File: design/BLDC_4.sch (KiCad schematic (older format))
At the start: 32 parts, among them K1 SERVO, P1 CANBUS, P10 MOTOR3, P11 MOTOR2, P12 MOTOR1, P2 HALL/Encoder, P3 HALL/Encoder, P4 PWR_COMM, P5 IN+, P6 IN-, P7 MOTOR3, P8 MOTOR2, P9 MOTOR1, X1 MINI-USB-SHIELD-32005-201

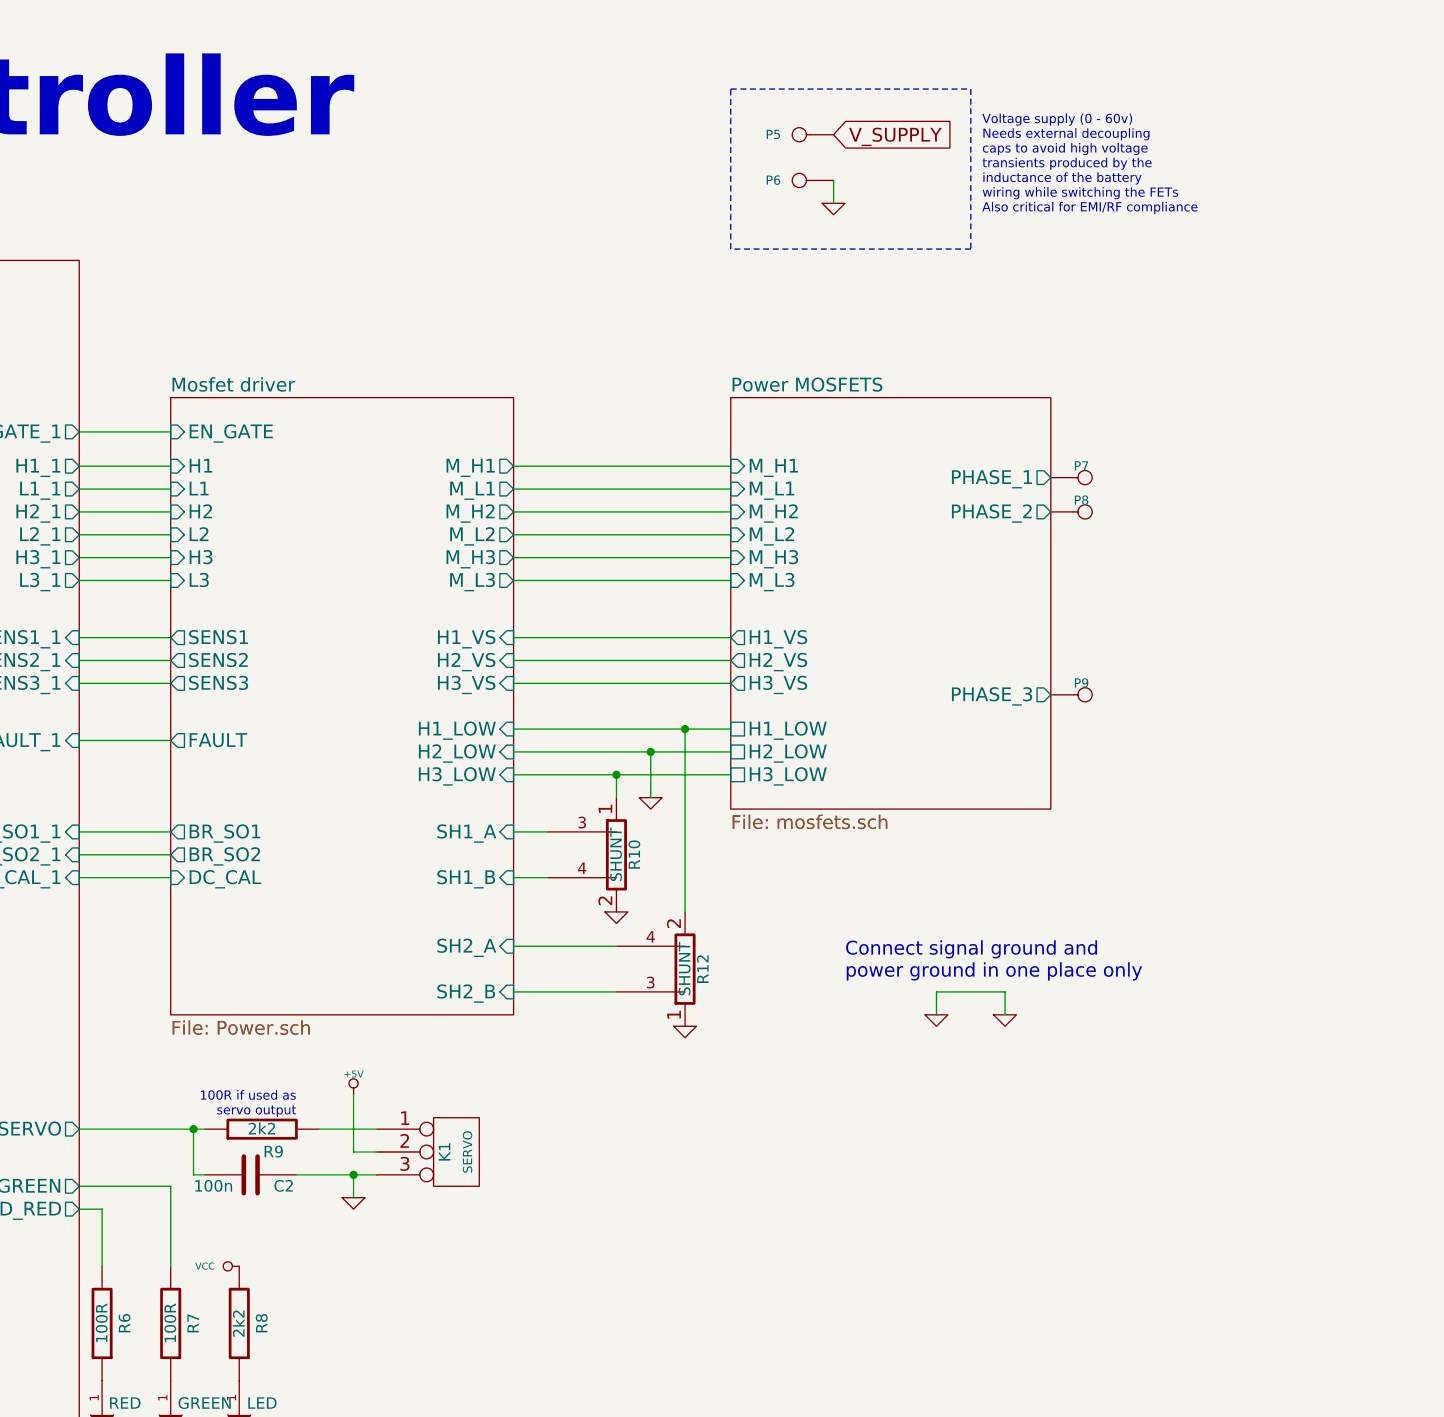
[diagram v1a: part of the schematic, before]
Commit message: Declare mosfet supply
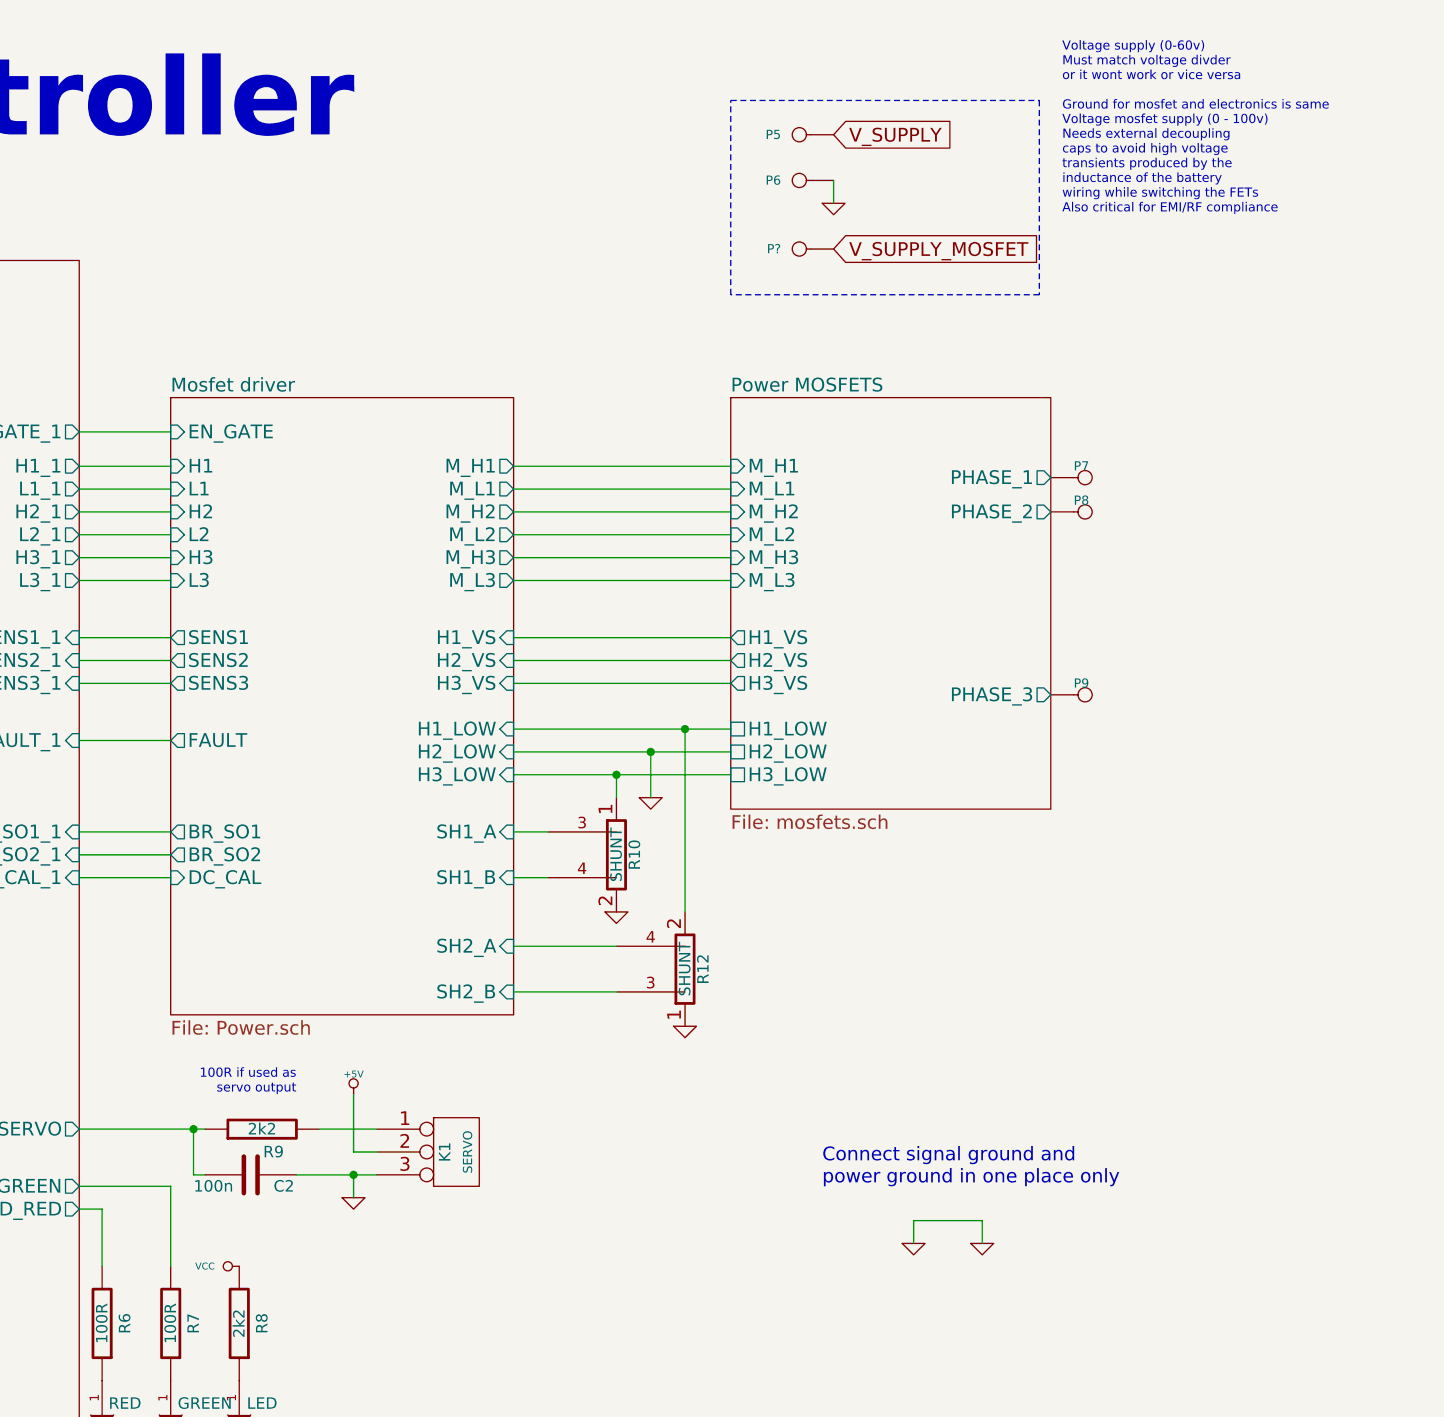
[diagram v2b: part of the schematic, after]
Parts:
- added P?: IN+, CRF1:1PAD_4x5mm, symbol CONN_1
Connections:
- new net V_SUPPLY_MOSFET: P?.1
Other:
- note added: "Voltage mosfet supply (0 - 100v)\nNeeds external decoupling\ncaps to avoid high voltage\ntransients produced by the\ninductance of the battery\nwiring while switching the FETs\nAlso critical for EMI/RF compliance"
- note added: "Voltage supply (0-60v)\nMust match voltage divder\nor it wont work or vice versa\n\nGround for mosfet and electronics is same"
- note removed: "Voltage supply (0 - 60v)\nNeeds external decoupling\ncaps to avoid high voltage\ntransients produced by the\ninductance of the battery\nwiring while switching the FETs\nAlso critical for EMI/RF compliance"
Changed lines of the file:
@@
 $EndComp
 $Comp
-L +5V #PWR01
+L +5V #PWR3
 U 1 1 522DA04D
 P 2850 5050
-F 0 "#PWR01" H 2850 5140 20  0001 C CNN
+F 0 "#PWR3" H 2850 5140 20  0001 C CNN
 F 1 "+5V" V 2800 5100 30  0000 C CNN
 F 2 "" H 2850 5050 60  0001 C CNN
@@
 $EndComp
 $Comp
-L GND #PWR02
+L GND #PWR6
 U 1 1 522DA053
 P 2900 4550
-F 0 "#PWR02" H 2900 4550 30  0001 C CNN
+F 0 "#PWR6" H 2900 4550 30  0001 C CNN
 F 1 "GND" H 2900 4480 30  0001 C CNN
 F 2 "" H 2900 4550 60  0001 C CNN
@@
 $EndComp
 $Comp
-L GND #PWR03
+L GND #PWR18
 U 1 1 522DA0BA
 P 8400 6000
-F 0 "#PWR03" H 8400 6000 30  0001 C CNN
+F 0 "#PWR18" H 8400 6000 30  0001 C CNN
 F 1 "GND" H 8400 5930 30  0001 C CNN
 F 2 "" H 8400 6000 60  0001 C CNN
@@
 V_SUPPLY
 $Comp
-L GND #PWR04
+L GND #PWR11
 U 1 1 522DA0CE
 P 3100 2650
-F 0 "#PWR04" H 3100 2650 30  0001 C CNN
+F 0 "#PWR11" H 3100 2650 30  0001 C CNN
 F 1 "GND" H 3100 2580 30  0001 C CNN
 F 2 "" H 3100 2650 60  0001 C CNN
@@
 $EndComp
 $Comp
-L GND #PWR05
+L GND #PWR5
 U 1 1 522DA0E2
 P 2850 6950
-F 0 "#PWR05" H 2850 6950 30  0001 C CNN
+F 0 "#PWR5" H 2850 6950 30  0001 C CNN
 F 1 "GND" H 2850 6880 30  0001 C CNN
 F 2 "" H 2850 6950 60  0001 C CNN
@@
 $EndComp
 $Comp
-L GND #PWR06
+L GND #PWR10
 U 1 1 522DA0FC
 P 3000 3600
-F 0 "#PWR06" H 3000 3600 30  0001 C CNN
+F 0 "#PWR10" H 3000 3600 30  0001 C CNN
 F 1 "GND" H 3000 3530 30  0001 C CNN
 F 2 "" H 3000 3600 60  0001 C CNN
@@
 $EndComp
 $Comp
-L +5V #PWR07
+L +5V #PWR8
 U 1 1 522DA11A
 P 2950 6750
-F 0 "#PWR07" H 2950 6840 20  0001 C CNN
+F 0 "#PWR8" H 2950 6840 20  0001 C CNN
 F 1 "+5V" V 2950 6900 30  0000 C CNN
 F 2 "" H 2950 6750 60  0001 C CNN
@@
 $EndComp
 $Comp
-L VCC #PWR08
+L VCC #PWR9
 U 1 1 522DA120
 P 2950 6850
-F 0 "#PWR08" H 2950 6950 30  0001 C CNN
+F 0 "#PWR9" H 2950 6950 30  0001 C CNN
 F 1 "VCC" V 2950 7000 30  0000 C CNN
 F 2 "" H 2950 6850 60  0001 C CNN
@@
 $EndComp
 $Comp
-L +5V #PWR09
+L +5V #PWR17
 U 1 1 522DA158
 P 8400 5550
-F 0 "#PWR09" H 8400 5640 20  0001 C CNN
+F 0 "#PWR17" H 8400 5640 20  0001 C CNN
 F 1 "+5V" H 8400 5640 30  0000 C CNN
 F 2 "" H 8400 5550 60  0001 C CNN
@@
 	-1   0    0    -1
 $EndComp
-Text Notes 8150 5650 2    40   ~ 0
+Text Notes 8150 5550 2    40   ~ 0
 100R if used as\nservo output
 $Comp
@@
 $EndComp
 $Comp
-L +5V #PWR010
+L +5V #PWR12
 U 1 1 522DA254
 P 4200 3050
-F 0 "#PWR010" H 4200 3140 20  0001 C CNN
+F 0 "#PWR12" H 4200 3140 20  0001 C CNN
 F 1 "+5V" H 4200 3140 30  0000 C CNN
 F 2 "" H 4200 3050 60  0001 C CNN
@@
 $EndComp
 $Comp
-L GND #PWR011
+L GND #PWR26
 U 1 1 53FA1F8F
-P 10950 5200
-F 0 "#PWR011" H 10950 5200 30  0001 C CNN
-F 1 "GND" H 10950 5130 30  0001 C CNN
-F 2 "" H 10950 5200 60  0001 C CNN
-F 3 "" H 10950 5200 60  0001 C CNN
-	1    10950 5200
+P 10850 6200
+F 0 "#PWR26" H 10850 6200 30  0001 C CNN
+F 1 "GND" H 10850 6130 30  0001 C CNN
+F 2 "" H 10850 6200 60  0001 C CNN
+F 3 "" H 10850 6200 60  0001 C CNN
+	1    10850 6200
 	1    0    0    -1
 $EndComp
@@
 C8 C8 08 D2 A9 87 39 1B F9 3D 64 10 3C A5 22 3B 19 76 2F 98 2B 2B 2B 1E 8F A7 AB AB 0B FB AC 1D
 B9 73 C8 EF 2C EC 8D 33 57 03 96 70 05 29 43 0C 6A C5 A8 D7 30 9E 87 2D DE BE E8 EA 73 2F 9C 18
-F1 B3 C3 9F 6D FA 1E FF 03 71 17 46 7E 55 DF FF 4E 00 00 00 00 49 45 4E 44 AE 42 60 82 35 $EndBitmap
+F1 B3 C3 9F 6D FA 1E FF 03 71 17 46 7E 55 DF FF 4E 00 00 00 00 49 45 4E 44 AE 42 60 82 1A $EndBitmap
 EndData
 $EndBitmap
@@
 $EndSheet
 $Comp
-L GND #PWR012
+L GND #PWR2
 U 1 1 53FB6DA8
 P 2850 4200
-F 0 "#PWR012" H 2850 4200 30  0001 C CNN
+F 0 "#PWR2" H 2850 4200 30  0001 C CNN
 F 1 "GND" H 2850 4130 30  0001 C CNN
 F 2 "" H 2850 4200 60  0001 C CNN
@@
 	0    1    1    0
 $EndComp
-Text Notes 11150 1700 0    40   ~ 0
-Voltage supply (0 - 60v)\nNeeds external decoupling\ncaps to avoid high voltage\ntransients produced by the\ninductance of the battery\nwiring while switching the FETs\nAlso critical for EMI/RF compliance
+Text Notes 11500 1700 0    40   ~ 0
+Voltage mosfet supply (0 - 100v)\nNeeds external decoupling\ncaps to avoid high voltage\ntransients produced by the\ninductance of the battery\nwiring while switching the FETs\nAlso critical for EMI/RF compliance
 $Comp
 L R R6
@@
 $EndComp
 $Comp
-L GND #PWR013
+L GND #PWR13
 U 1 1 53FC021C
 P 7300 7200
-F 0 "#PWR013" H 7300 7200 30  0001 C CNN
+F 0 "#PWR13" H 7300 7200 30  0001 C CNN
 F 1 "GND" H 7300 7130 30  0001 C CNN
 F 2 "" H 7300 7200 60  0001 C CNN
@@
 $EndComp
 $Comp
-L GND #PWR014
+L GND #PWR14
 U 1 1 53FC131A
 P 7600 7200
-F 0 "#PWR014" H 7600 7200 30  0001 C CNN
+F 0 "#PWR14" H 7600 7200 30  0001 C CNN
 F 1 "GND" H 7600 7130 30  0001 C CNN
 F 2 "" H 7600 7200 60  0001 C CNN
@@
 $EndComp
 $Comp
-L GND #PWR015
+L GND #PWR16
 U 1 1 53FC8AA4
 P 7900 7200
-F 0 "#PWR015" H 7900 7200 30  0001 C CNN
+F 0 "#PWR16" H 7900 7200 30  0001 C CNN
 F 1 "GND" H 7900 7130 30  0001 C CNN
 F 2 "" H 7900 7200 60  0001 C CNN
@@
 $EndComp
 $Comp
-L VCC #PWR016
+L VCC #PWR15
 U 1 1 53FC98D2
 P 7900 6300
-F 0 "#PWR016" H 7900 6400 30  0001 C CNN
+F 0 "#PWR15" H 7900 6400 30  0001 C CNN
 F 1 "VCC" V 7900 6450 30  0000 C CNN
 F 2 "" H 7900 6300 60  0001 C CNN
@@
 Connection ~ 9700 4050
 Wire Wire Line
-	10950 5100 10950 5200
+	10850 6100 10850 6200
 Wire Wire Line
-	11250 5100 11250 5200
+	11150 6100 11150 6200
 Wire Wire Line
 	10500 1650 10500 1550
@@
 Wire Wire Line
 	4050 3300 4650 3300
-Wire Notes Line
-	10050 1150 11100 1150
-Wire Notes Line
-	11100 1150 11100 1850
-Wire Notes Line
-	11100 1850 10050 1850
-Wire Notes Line
-	10050 1850 10050 1150
 Wire Wire Line
 	7300 6050 7300 6300
@@
 $EndComp
 $Comp
-L +5V #PWR017
+L +5V #PWR1
 U 1 1 54036995
 P 2850 3900
-F 0 "#PWR017" H 2850 3990 20  0001 C CNN
+F 0 "#PWR1" H 2850 3990 20  0001 C CNN
 F 1 "+5V" H 2850 3990 30  0000 C CNN
 F 2 "" H 2850 3900 60  0001 C CNN
@@
 $EndComp
 Wire Wire Line
-	10950 5100 11250 5100
+	10850 6100 11150 6100
 Wire Wire Line
 	4250 7550 4650 7550
@@
 $EndComp
 $Comp
-L GND #PWR018
+L GND #PWR27
 U 1 1 548F24DF
-P 11250 5200
-F 0 "#PWR018" H 11250 5200 30  0001 C CNN
-F 1 "GND" H 11250 5130 30  0001 C CNN
-F 2 "" H 11250 5200 60  0001 C CNN
-F 3 "" H 11250 5200 60  0001 C CNN
-	1    11250 5200
+P 11150 6200
+F 0 "#PWR27" H 11150 6200 30  0001 C CNN
+F 1 "GND" H 11150 6130 30  0001 C CNN
+F 2 "" H 11150 6200 60  0001 C CNN
+F 3 "" H 11150 6200 60  0001 C CNN
+	1    11150 6200
 	1    0    0    -1
 $EndComp
 $Comp
-L GND #PWR019
+L GND #PWR23
 U 1 1 548F2504
 P 9850 5250
-F 0 "#PWR019" H 9850 5250 30  0001 C CNN
+F 0 "#PWR23" H 9850 5250 30  0001 C CNN
 F 1 "GND" H 9850 5180 30  0001 C CNN
 F 2 "" H 9850 5250 60  0001 C CNN
@@
 $EndComp
 $Comp
-L GND #PWR020
+L GND #PWR19
 U 1 1 548F2529
 P 9550 4750
-F 0 "#PWR020" H 9550 4750 30  0001 C CNN
+F 0 "#PWR19" H 9550 4750 30  0001 C CNN
 F 1 "GND" H 9550 4680 30  0001 C CNN
 F 2 "" H 9550 4750 60  0001 C CNN
@@
 $EndComp
 $Comp
-L GND #PWR021
+L GND #PWR21
 U 1 1 548F254E
 P 9700 4250
-F 0 "#PWR021" H 9700 4250 30  0001 C CNN
+F 0 "#PWR21" H 9700 4250 30  0001 C CNN
 F 1 "GND" H 9700 4180 30  0001 C CNN
 F 2 "" H 9700 4250 60  0001 C CNN
@@
 $EndComp
 $Comp
-L GND #PWR022
+L GND #PWR25
 U 1 1 548F2573
 P 10500 1650
-F 0 "#PWR022" H 10500 1650 30  0001 C CNN
+F 0 "#PWR25" H 10500 1650 30  0001 C CNN
 F 1 "GND" H 10500 1580 30  0001 C CNN
 F 2 "" H 10500 1650 60  0001 C CNN
@@
 	1    0    0    -1
 $EndComp
-Text Notes 10550 5050 0    60   ~ 0
+Text Notes 10450 5950 0    60   ~ 0
 Connect signal ground and\npower ground in one place only
 $Comp
@@
 $EndComp
 $Comp
-L +5V #PWR023
+L +5V #PWR4
 U 1 1 54B6A9FD
 P 2850 6100
-F 0 "#PWR023" H 2850 6190 20  0001 C CNN
+F 0 "#PWR4" H 2850 6190 20  0001 C CNN
 F 1 "+5V" V 2800 6150 30  0000 C CNN
 F 2 "" H 2850 6100 60  0001 C CNN
@@
 $EndComp
 $Comp
-L GND #PWR024
+L GND #PWR7
 U 1 1 54B6AA03
 P 2900 5600
-F 0 "#PWR024" H 2900 5600 30  0001 C CNN
+F 0 "#PWR7" H 2900 5600 30  0001 C CNN
 F 1 "GND" H 2900 5530 30  0001 C CNN
 F 2 "" H 2900 5600 60  0001 C CNN
@@
 C8 C8 08 D2 A9 87 39 1B F9 3D 64 10 3C A5 22 3B 19 76 2F 98 2B 2B 2B 1E 8F A7 AB AB 0B FB AC 1D
 B9 73 C8 EF 2C EC 8D 33 57 03 96 70 05 29 43 0C 6A C5 A8 D7 30 9E 87 2D DE BE E8 EA 73 2F 9C 18
-F1 B3 C3 9F 6D FA 1E FF 03 71 17 46 7E 55 DF FF 4E 00 00 00 00 49 45 4E 44 AE 42 60 82 35 $EndBitmap
+F1 B3 C3 9F 6D FA 1E FF 03 71 17 46 7E 55 DF FF 4E 00 00 00 00 49 45 4E 44 AE 42 60 82 1A $EndBitmap
 EndData
 $EndBitmap
@@
 $EndComp
 $Comp
-L GND #PWR025
+L GND #PWR24
 U 1 1 54B73612
 P 9850 10800
-F 0 "#PWR025" H 9850 10800 30  0001 C CNN
+F 0 "#PWR24" H 9850 10800 30  0001 C CNN
 F 1 "GND" H 9850 10730 30  0001 C CNN
 F 2 "" H 9850 10800 60  0001 C CNN
@@
 $EndComp
 $Comp
-L GND #PWR026
+L GND #PWR20
 U 1 1 54B73618
 P 9550 10300
-F 0 "#PWR026" H 9550 10300 30  0001 C CNN
+F 0 "#PWR20" H 9550 10300 30  0001 C CNN
 F 1 "GND" H 9550 10230 30  0001 C CNN
 F 2 "" H 9550 10300 60  0001 C CNN
@@
 $EndComp
 $Comp
-L GND #PWR027
+L GND #PWR22
 U 1 1 54B7361E
 P 9700 9800
-F 0 "#PWR027" H 9700 9800 30  0001 C CNN
+F 0 "#PWR22" H 9700 9800 30  0001 C CNN
 F 1 "GND" H 9700 9730 30  0001 C CNN
 F 2 "" H 9700 9800 60  0001 C CNN
@@
 F31 "SH2_B" I R 9100 10650 60
 $EndSheet
+Text Notes 11500 1250 0    40   ~ 0
+Voltage supply (0-60v)\nMust match voltage divder\nor it wont work or vice versa\n\nGround for mosfet and electronics is same
+$Comp
+L CONN_1 P?
+U 1 1 54D705F4
+P 10350 1850
+F 0 "P?" H 10430 1850 40  0000 L CNN
+F 1 "IN+" H 10350 1905 30  0001 C CNN
+F 2 "CRF1:1PAD_4x5mm" H 10350 1850 60  0001 C CNN
+F 3 "" H 10350 1850 60  0001 C CNN
+	1    10350 1850
+	-1   0    0    1
+$EndComp
+Text GLabel 10500 1850 2    60   Input ~ 0
+V_SUPPLY_MOSFET
+Wire Notes Line
+	10050 1200 11400 1200
+Wire Notes Line
+	11400 1200 11400 2050
+Wire Notes Line
+	11400 2050 10050 2050
+Wire Notes Line
+	10050 2050 10050 1200
 $EndSCHEMATC
